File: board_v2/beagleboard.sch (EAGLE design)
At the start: 24 parts, among them U1 DWM1000, X1 5566-2

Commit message: schematiccomplete
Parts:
- removed R7, R8, R9: 0R, rcl:R-EU_R0603
- added IMUCON: B4B-ZR, jst:B4B-ZR
- added X2: 04-JST-B4B-XH-A, bt_con-jst-xh:04-JST-B4B-XH-A
- R4, R5, R6: value 0R -> (none); device rcl:R-EU_R0603 -> rcl:R-EU_R0805
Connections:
- removed net N$10: MOTORL.3, R9.2
- removed net N$11: MOTORL.4, R8.2
- removed net N$4: MOTOTR.2, R4.2
- removed net N$47: U$1.GPIO_45
- removed net N$48: U$1.GPIO_23
- removed net N$49: U$1.GPIO_47
- removed net N$50: U$1.GPIO_27
- removed net N$51: U$1.GPIO_22
- removed net N$52: U$1.GPIO_62
- removed net N$7: MOTOTR.3, R5.2
- removed net N$73: U$1.I2C1_SDA
- removed net N$8: MOTOTR.4, R6.2
- removed net N$82: U$1.AIN5
- removed net N$83: U$1.AIN3
- removed net N$84: U$1.AIN1
- removed net N$9: MOTORL.2, R7.2
- removed net N$96: U$1.I2C1_SCL
- removed net WIPOWER: REGCON.1
- new net CELL1: R4.2, U$1.AIN5, X2-3.1
- new net CELL2: R5.2, U$1.AIN3, X2-2.1
- new net CELL3: R6.2, U$1.AIN1, X2-1.1
- new net MLM0: MOTORL.2, U$1.GPIO_45
- new net MLM1: MOTORL.3, U$1.GPIO_23
- new net MLM2: MOTORL.4, U$1.GPIO_47
- new net MRM0: MOTOTR.2, U$1.GPIO_27
- new net MRM1: MOTOTR.3, U$1.GPIO_22
- new net MRM2: MOTOTR.4, U$1.GPIO_62
- new net SCL1: IMUCON.3, U$1.I2C1_SCL
- new net SDA1: IMUCON.2, U$1.I2C1_SDA
- net +5V: now also IMUCON.1; no longer R4.1, R5.1, R6.1, R7.1, R8.1, R9.1
- net GND: now also IMUCON.4, R4.1, R5.1, R6.1, X2-4.1
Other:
- moved on the sheet: R4, R5, R6

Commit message: main wires
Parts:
- added R7, R8, R9: (no value), rcl:R-EU_R0805
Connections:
- removed net N$17: MCONL.2, MOTORL1.5
- removed net N$19: MCONR.4, MOTORR1.4
- removed net N$20: MCONR.3, MOTORR1.3
- new net N$10: MCONL.1, MOTORL1.5
- new net N$11: MCONL.4, MOTORL1.3
- new net N$4: R7.2, X2-1.1
- new net N$7: R8.2, X2-2.1
- new net N$8: R9.2, X2-3.1
- new net N$9: MCONL.2, MOTORL1.6
- net +3V3: no longer C2.+, REGCON.4
- net +5V: now also C2.+, REGCON.4
- net CELL1: now also R9.1; no longer X2-3.1
- net CELL2: now also R8.1; no longer X2-2.1
- net CELL3: now also R7.1; no longer X2-1.1
- net MRDIR: now also U$1.GPIO_60; no longer U$1.GPIO_51
- net MREN: now also U$1.GPIO_51; no longer U$1.GPIO_60
- net MRM1: now also U$1.GPIO_62; no longer U$1.GPIO_22
- net MRM2: now also U$1.GPIO_22; no longer U$1.GPIO_62
- net N$1: now also MCONL.3; no longer MCONL.4
- net N$12: now also MCONR.2; no longer MCONR.1
- net N$13: now also MCONR.3, MOTORR1.4; no longer MCONL.3, MOTORL1.3
- net N$14: now also MCONR.4, MOTORR1.3; no longer MCONL.1, MOTORL1.6
- net N$15: now also MCONR.1; no longer MCONR.2
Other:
- moved on the sheet: X2-1, X2-2, X2-3, X2-4

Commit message: boardv2 ready to check
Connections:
- net +3V3: no longer U$1.VDD_3V3EXP@1, U$1.VDD_3V3EXP@2
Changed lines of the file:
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@@
 <part name="GND7" library="supply1" deviceset="GND" device=""/>
 <part name="GND8" library="supply1" deviceset="GND" device=""/>
-<part name="+3V1" library="supply1" deviceset="+3V3" device=""/>
 <part name="P+6" library="supply1" deviceset="+5V" device=""/>
-<part name="+3V2" library="supply1" deviceset="+3V3" device=""/>
 <part name="X1" library="con-molex" deviceset="5566-2" device=""/>
 <part name="+3V4" library="supply1" deviceset="+3V3" device=""/>
@@
 <instance part="GND7" gate="1" x="220.98" y="116.84"/>
 <instance part="GND8" gate="1" x="124.46" y="116.84"/>
-<instance part="+3V1" gate="G$1" x="215.9" y="58.42"/>
 <instance part="P+6" gate="1" x="121.92" y="58.42"/>
-<instance part="+3V2" gate="G$1" x="129.54" y="58.42"/>
 <instance part="X1" gate="-1" x="-17.78" y="101.6" rot="R180"/>
 <instance part="X1" gate="-2" x="-17.78" y="106.68" rot="R180"/>
@@
 </segment>
 <segment>
-<pinref part="U$1" gate="G$1" pin="VDD_3V3EXP@1"/>
-<wire x1="144.78" y1="50.8" x2="129.54" y2="50.8" width="0.1524" layer="91"/>
-<wire x1="129.54" y1="50.8" x2="129.54" y2="55.88" width="0.1524" layer="91"/>
-<pinref part="+3V2" gate="G$1" pin="+3V3"/>
-</segment>
-<segment>
-<pinref part="U$1" gate="G$1" pin="VDD_3V3EXP@2"/>
-<wire x1="200.66" y1="50.8" x2="215.9" y2="50.8" width="0.1524" layer="91"/>
-<pinref part="+3V1" gate="G$1" pin="+3V3"/>
-<wire x1="215.9" y1="50.8" x2="215.9" y2="55.88" width="0.1524" layer="91"/>
-</segment>
-<segment>

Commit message: added distance sensor connectors
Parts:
- added SENS1, SENS3, SENS4: B4B-ZR, jst:B4B-ZR
- renumbered IMUCON to SENS2
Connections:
- removed net N$100: U$1.GPIO_117
- removed net N$74: U$1.I2C2_SDA
- removed net N$75: U$1.UART2_RXD
- removed net N$76: U$1.UART1_TXD
- removed net N$77: U$1.UART1_RXD
- removed net N$97: U$1.I2C2_SCL
- removed net N$98: U$1.UART2_TXD
- removed net N$99: U$1.GPIO_49
- new net D1ECHO: SENS1.3, U$1.UART1_TXD
- new net D1TRIG: SENS1.4, U$1.UART1_RXD
- new net D2ECHO: SENS2.3, U$1.UART2_TXD
- new net D2TRIG: SENS2.4, U$1.UART2_RXD
- new net D3ECHO: SENS3.3, U$1.GPIO_49
- new net D3TRIG: SENS3.4, U$1.GPIO_117
- new net D4ECHO: SENS4.3, U$1.I2C2_SCL
- new net D4TRIG: SENS4.4, U$1.I2C2_SDA
- net +5V: now also SENS1.1, SENS3.1, SENS4.1
- net GND: now also SENS1.2, SENS2.2, SENS3.2, SENS4.2; no longer SENS2.4
- net SCL1: no longer SENS2.3
- net SDA1: no longer SENS2.2
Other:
- moved on the sheet: R4, R5, R6, R7, R8, R9, X2-1, X2-2, X2-3, X2-4

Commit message: gpioadjustment
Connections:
- removed net N$105: U$1.AIN6
- removed net N$106: U$1.AIN2
- removed net N$107: U$1.AIN0
- removed net N$45: U$1.TIMER4
- removed net N$46: U$1.TIMER5
- removed net N$69: U$1.SYS_RESETN
- removed net N$92: U$1.PWR_BUT
- new net N$17: U$1.GPIO_22
- new net N$19: U$1.GPIO_62
- net +3V3: no longer U$1.VDD_ADC
- net D3TRIG: now also U$1.AIN6; no longer U$1.GPIO_117
- net D4ECHO: now also U$1.AIN0; no longer U$1.I2C2_SCL
- net D4TRIG: now also U$1.AIN2; no longer U$1.I2C2_SDA
- net MLM0: now also U$1.TIMER4; no longer U$1.GPIO_45
- net MLM1: now also U$1.TIMER5; no longer U$1.GPIO_23
- net MLM2: now also U$1.GPIO_45; no longer U$1.GPIO_47
- net MRM0: now also U$1.GPIO_23; no longer U$1.GPIO_27
- net MRM1: now also U$1.GPIO_47; no longer U$1.GPIO_62
- net MRM2: now also U$1.GPIO_27; no longer U$1.GPIO_22
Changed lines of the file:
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@@
 <?xml version="1.0" encoding="utf-8"?>
 <!DOCTYPE eagle SYSTEM "eagle.dtd">
-<eagle version="7.1.0">
+<eagle version="7.7.0">
 <drawing>
 <settings>
@@
 <part name="P+6" library="supply1" deviceset="+5V" device=""/>
 <part name="X1" library="con-molex" deviceset="5566-2" device=""/>
-<part name="+3V4" library="supply1" deviceset="+3V3" device=""/>
 <part name="SENS2" library="jst" deviceset="B4B-ZR" device=""/>
 <part name="P+7" library="supply1" deviceset="+5V" device=""/>
@@
 <instance part="X1" gate="-1" x="-17.78" y="101.6" rot="R180"/>
 <instance part="X1" gate="-2" x="-17.78" y="106.68" rot="R180"/>
-<instance part="+3V4" gate="G$1" x="220.98" y="20.32"/>
 <instance part="SENS2" gate="G$1" x="71.12" y="116.84" rot="R90"/>
 <instance part="P+7" gate="1" x="63.5" y="106.68"/>
@@
 <junction x="60.96" y="71.12"/>
 </segment>
-<segment>
-<pinref part="U$1" gate="G$1" pin="VDD_ADC"/>
-<wire x1="200.66" y1="15.24" x2="220.98" y2="15.24" width="0.1524" layer="91"/>
-<wire x1="220.98" y1="15.24" x2="220.98" y2="17.78" width="0.1524" layer="91"/>
-<pinref part="+3V4" gate="G$1" pin="+3V3"/>
-</segment>
 </net>
 <net name="N$2" class="0">
@@
 </segment>
 <segment>
+<pinref part="U$1" gate="G$1" pin="GPIO_23"/>
+<wire x1="144.78" y1="104.14" x2="134.62" y2="104.14" width="0.1524" layer="91"/>
+<label x="134.62" y="104.14" size="1.27" layer="95" rot="R180" xref="yes"/>
+</segment>
+</net>
+<net name="MRM1" class="0">
+<segment>
+<pinref part="MOTOTR" gate="A" pin="3"/>
+<wire x1="58.42" y1="-5.08" x2="66.04" y2="-5.08" width="0.1524" layer="91"/>
+<label x="58.42" y="-5.08" size="1.27" layer="95" rot="R180" xref="yes"/>
+</segment>
+<segment>
+<pinref part="U$1" gate="G$1" pin="GPIO_47"/>
+<wire x1="144.78" y1="101.6" x2="134.62" y2="101.6" width="0.1524" layer="91"/>
+<label x="134.62" y="101.6" size="1.27" layer="95" rot="R180" xref="yes"/>
+</segment>
+</net>
+<net name="MRM2" class="0">
+<segment>
+<pinref part="MOTOTR" gate="A" pin="4"/>
+<wire x1="58.42" y1="-7.62" x2="66.04" y2="-7.62" width="0.1524" layer="91"/>
+<label x="58.42" y="-7.62" size="1.27" layer="95" rot="R180" xref="yes"/>
+</segment>
+<segment>
 <pinref part="U$1" gate="G$1" pin="GPIO_27"/>
 <wire x1="144.78" y1="99.06" x2="134.62" y2="99.06" width="0.1524" layer="91"/>
@@
 </segment>
 </net>
-<net name="MRM1" class="0">
-<segment>
-<pinref part="MOTOTR" gate="A" pin="3"/>
-<wire x1="58.42" y1="-5.08" x2="66.04" y2="-5.08" width="0.1524" layer="91"/>
-<label x="58.42" y="-5.08" size="1.27" layer="95" rot="R180" xref="yes"/>
-</segment>
-<segment>
-<pinref part="U$1" gate="G$1" pin="GPIO_62"/>
-<wire x1="144.78" y1="93.98" x2="134.62" y2="93.98" width="0.1524" layer="91"/>
-<label x="134.62" y="93.98" size="1.27" layer="95" rot="R180" xref="yes"/>
-</segment>
-</net>
-<net name="MRM2" class="0">
-<segment>
-<pinref part="MOTOTR" gate="A" pin="4"/>
-<wire x1="58.42" y1="-7.62" x2="66.04" y2="-7.62" width="0.1524" layer="91"/>
-<label x="58.42" y="-7.62" size="1.27" layer="95" rot="R180" xref="yes"/>
-</segment>
-<segment>
-<pinref part="U$1" gate="G$1" pin="GPIO_22"/>
-<wire x1="144.78" y1="96.52" x2="134.62" y2="96.52" width="0.1524" layer="91"/>
-<label x="134.62" y="96.52" size="1.27" layer="95" rot="R180" xref="yes"/>
-</segment>
-</net>
 <net name="MLM0" class="0">
 <segment>
@@
 </segment>
 <segment>
+<pinref part="U$1" gate="G$1" pin="TIMER4"/>
+<wire x1="144.78" y1="111.76" x2="134.62" y2="111.76" width="0.1524" layer="91"/>
+<label x="134.62" y="111.76" size="1.27" layer="95" rot="R180" xref="yes"/>
+</segment>
+</net>
+<net name="MLM1" class="0">
+<segment>
+<pinref part="MOTORL" gate="A" pin="3"/>
+<wire x1="-2.54" y1="-5.08" x2="5.08" y2="-5.08" width="0.1524" layer="91"/>
+<label x="-2.54" y="-5.08" size="1.27" layer="95" rot="R180" xref="yes"/>
+</segment>
+<segment>
+<pinref part="U$1" gate="G$1" pin="TIMER5"/>
+<wire x1="144.78" y1="109.22" x2="134.62" y2="109.22" width="0.1524" layer="91"/>
+<label x="134.62" y="109.22" size="1.27" layer="95" rot="R180" xref="yes"/>
+</segment>
+</net>
+<net name="MLM2" class="0">
+<segment>
+<pinref part="MOTORL" gate="A" pin="4"/>
+<wire x1="-2.54" y1="-7.62" x2="5.08" y2="-7.62" width="0.1524" layer="91"/>
+<label x="-2.54" y="-7.62" size="1.27" layer="95" rot="R180" xref="yes"/>
+</segment>
+<segment>
 <pinref part="U$1" gate="G$1" pin="GPIO_45"/>
 <wire x1="144.78" y1="106.68" x2="134.62" y2="106.68" width="0.1524" layer="91"/>
@@
 </segment>
 </net>
-<net name="MLM1" class="0">
-<segment>
-<pinref part="MOTORL" gate="A" pin="3"/>
-<wire x1="-2.54" y1="-5.08" x2="5.08" y2="-5.08" width="0.1524" layer="91"/>
-<label x="-2.54" y="-5.08" size="1.27" layer="95" rot="R180" xref="yes"/>
-</segment>
-<segment>
-<pinref part="U$1" gate="G$1" pin="GPIO_23"/>
-<wire x1="144.78" y1="104.14" x2="134.62" y2="104.14" width="0.1524" layer="91"/>
-<label x="134.62" y="104.14" size="1.27" layer="95" rot="R180" xref="yes"/>
-</segment>
-</net>
-<net name="MLM2" class="0">
-<segment>
-<pinref part="MOTORL" gate="A" pin="4"/>
-<wire x1="-2.54" y1="-7.62" x2="5.08" y2="-7.62" width="0.1524" layer="91"/>
-<label x="-2.54" y="-7.62" size="1.27" layer="95" rot="R180" xref="yes"/>
-</segment>
-<segment>
-<pinref part="U$1" gate="G$1" pin="GPIO_47"/>
-<wire x1="144.78" y1="101.6" x2="134.62" y2="101.6" width="0.1524" layer="91"/>
-<label x="134.62" y="101.6" size="1.27" layer="95" rot="R180" xref="yes"/>
-</segment>
-</net>
 <net name="N$18" class="0">
 <segment>
@@
 </segment>
 </net>
-<net name="N$45" class="0">
-<segment>
-<pinref part="U$1" gate="G$1" pin="TIMER4"/>
-<wire x1="144.78" y1="111.76" x2="134.62" y2="111.76" width="0.1524" layer="91"/>
-</segment>
-</net>
-<net name="N$46" class="0">
-<segment>
-<pinref part="U$1" gate="G$1" pin="TIMER5"/>
-<wire x1="144.78" y1="109.22" x2="134.62" y2="109.22" width="0.1524" layer="91"/>
-</segment>
-</net>
 <net name="N$53" class="0">
 <segment>
@@
 </segment>
 </net>
-<net name="N$69" class="0">
-<segment>
-<pinref part="U$1" gate="G$1" pin="SYS_RESETN"/>
-<wire x1="200.66" y1="43.18" x2="210.82" y2="43.18" width="0.1524" layer="91"/>
-</segment>
-</net>
 <net name="D4TRIG" class="0">
-<segment>
-<pinref part="U$1" gate="G$1" pin="I2C2_SDA"/>
-<wire x1="200.66" y1="30.48" x2="210.82" y2="30.48" width="0.1524" layer="91"/>
-<label x="210.82" y="30.48" size="1.016" layer="95" xref="yes"/>
-</segment>
 <segment>
 <pinref part="SENS4" gate="G$1" pin="4"/>
 <wire x1="116.84" y1="109.22" x2="116.84" y2="104.14" width="0.1524" layer="91"/>
 <label x="116.84" y="104.14" size="1.016" layer="95" rot="R270" xref="yes"/>
+</segment>
+<segment>
+<pinref part="U$1" gate="G$1" pin="AIN2"/>
+<wire x1="144.78" y1="7.62" x2="134.62" y2="7.62" width="0.1524" layer="91"/>
+<label x="134.62" y="7.62" size="1.27" layer="95" rot="R180" xref="yes"/>
 </segment>
 </net>
@@
 </segment>
 </net>
-<net name="N$92" class="0">
-<segment>
-<pinref part="U$1" gate="G$1" pin="PWR_BUT"/>
-<wire x1="144.78" y1="43.18" x2="134.62" y2="43.18" width="0.1524" layer="91"/>
-</segment>
-</net>
 <net name="D4ECHO" class="0">
-<segment>
-<pinref part="U$1" gate="G$1" pin="I2C2_SCL"/>
-<wire x1="144.78" y1="30.48" x2="134.62" y2="30.48" width="0.1524" layer="91"/>
-<label x="134.62" y="30.48" size="1.016" layer="95" rot="R180" xref="yes"/>
-</segment>
 <segment>
 <pinref part="SENS4" gate="G$1" pin="3"/>
@@
 <label x="114.3" y="104.14" size="1.016" layer="95" rot="R270" xref="yes"/>
 </segment>
+<segment>
+<pinref part="U$1" gate="G$1" pin="AIN0"/>
+<wire x1="144.78" y1="5.08" x2="134.62" y2="5.08" width="0.1524" layer="91"/>
+<label x="134.62" y="5.08" size="1.27" layer="95" rot="R180" xref="yes"/>
+</segment>
 </net>
 <net name="D2ECHO" class="0">
@@
 </segment>
 <segment>
-<pinref part="U$1" gate="G$1" pin="GPIO_117"/>
-<wire x1="144.78" y1="22.86" x2="134.62" y2="22.86" width="0.1524" layer="91"/>
-<label x="134.62" y="22.86" size="1.016" layer="95" rot="R180" xref="yes"/>
+<pinref part="U$1" gate="G$1" pin="AIN6"/>
+<wire x1="144.78" y1="10.16" x2="134.62" y2="10.16" width="0.1524" layer="91"/>
+<label x="134.62" y="10.16" size="1.27" layer="95" rot="R180" xref="yes"/>
 </segment>
 </net>
@@
 <pinref part="U$1" gate="G$1" pin="AIN4"/>
 <wire x1="144.78" y1="12.7" x2="134.62" y2="12.7" width="0.1524" layer="91"/>
-</segment>
-</net>
-<net name="N$105" class="0">
-<segment>
-<pinref part="U$1" gate="G$1" pin="AIN6"/>
-<wire x1="144.78" y1="10.16" x2="134.62" y2="10.16" width="0.1524" layer="91"/>
-</segment>
-</net>
-<net name="N$106" class="0">
-<segment>
-<pinref part="U$1" gate="G$1" pin="AIN2"/>
-<wire x1="144.78" y1="7.62" x2="134.62" y2="7.62" width="0.1524" layer="91"/>
-</segment>
-</net>
-<net name="N$107" class="0">
-<segment>
-<pinref part="U$1" gate="G$1" pin="AIN0"/>
-<wire x1="144.78" y1="5.08" x2="134.62" y2="5.08" width="0.1524" layer="91"/>
 </segment>
 </net>
@@
 </segment>
 </net>
+<net name="N$17" class="0">
+<segment>
+<pinref part="U$1" gate="G$1" pin="GPIO_22"/>
+<wire x1="144.78" y1="96.52" x2="134.62" y2="96.52" width="0.1524" layer="91"/>
+</segment>
+</net>
+<net name="N$19" class="0">
+<segment>
+<pinref part="U$1" gate="G$1" pin="GPIO_62"/>
+<wire x1="144.78" y1="93.98" x2="134.62" y2="93.98" width="0.1524" layer="91"/>
+</segment>
+</net>

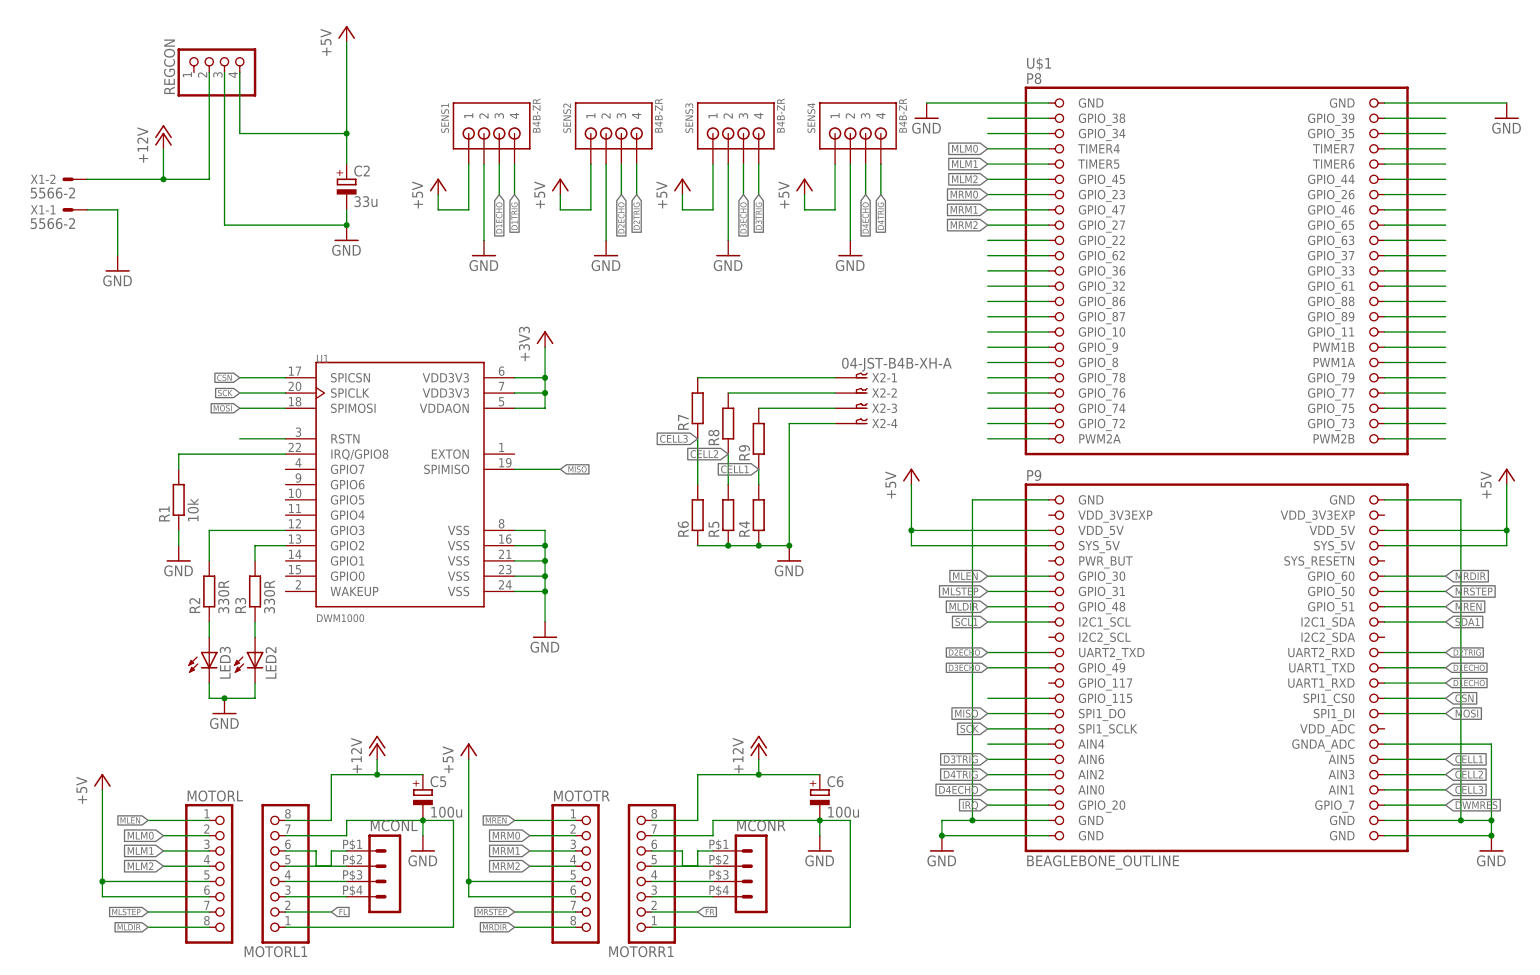
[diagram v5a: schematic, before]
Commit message: check and reconfigure gpios
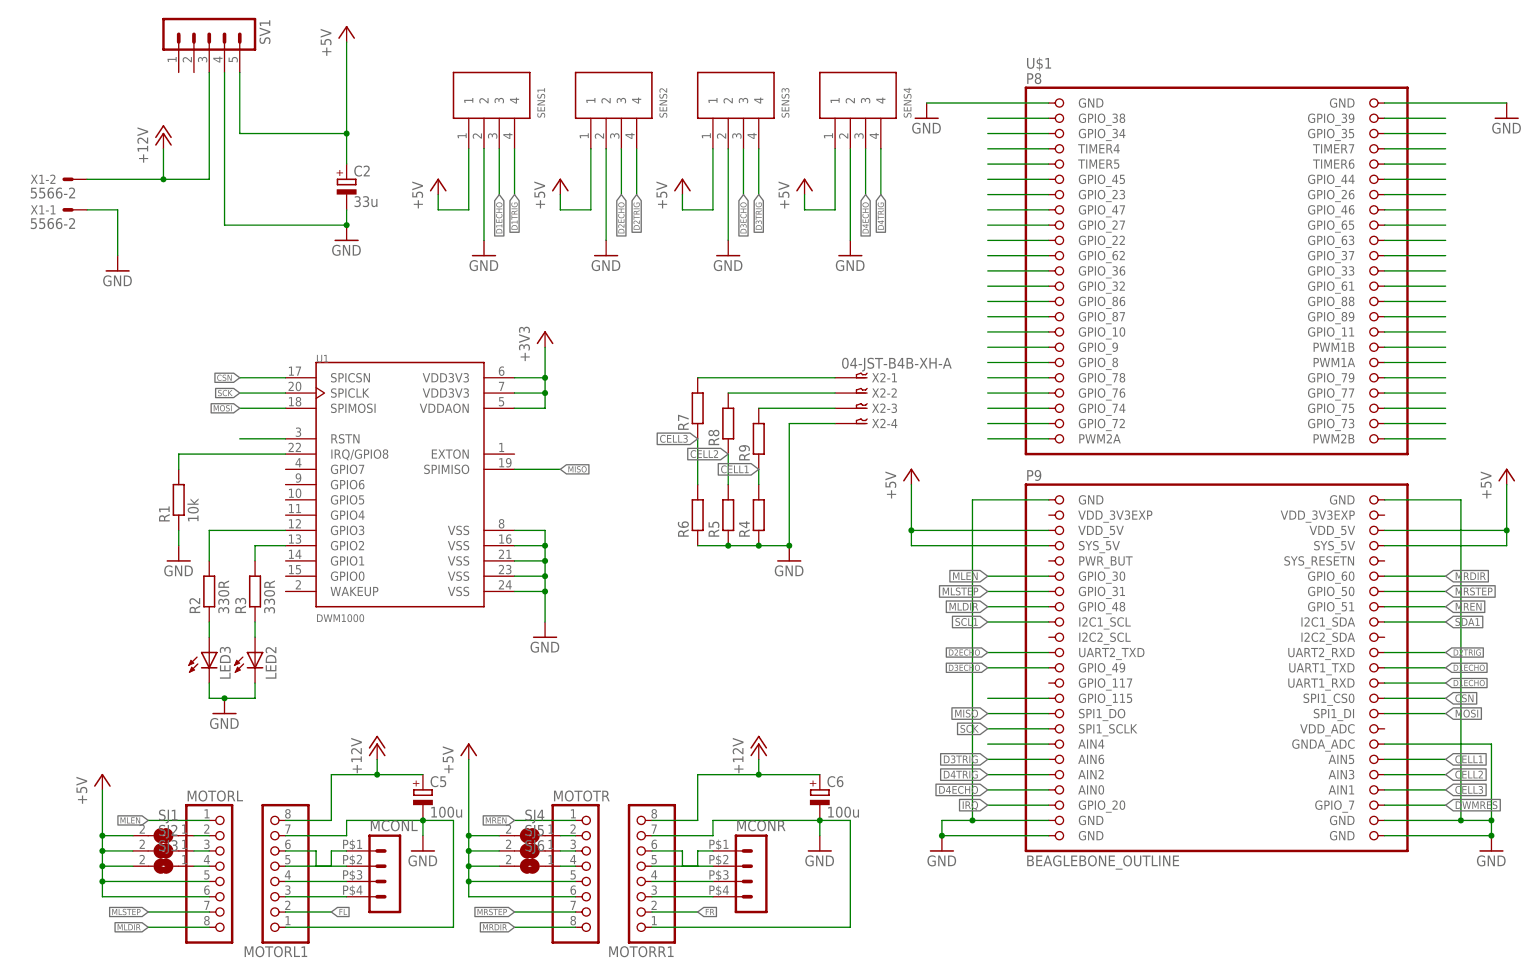
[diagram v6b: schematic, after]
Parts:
- removed REGCON: (no value), pinhead:PINHD-1X4
- added SJ1, SJ2, SJ3, SJ4, SJ5, SJ6: (no value), jumper:SJ
- added SV1: (no value), con-lstb:MA05-1
- SENS1, SENS2, SENS3, SENS4: value B4B-ZR -> 4PIN; device jst:B4B-ZR -> libsjst_eph:4PIN
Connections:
- removed net MLM0: MOTORL.2, U$1.TIMER4
- removed net MLM1: MOTORL.3, U$1.TIMER5
- removed net MLM2: MOTORL.4, U$1.GPIO_45
- removed net MRM0: MOTOTR.2, U$1.GPIO_23
- removed net MRM1: MOTOTR.3, U$1.GPIO_47
- removed net MRM2: MOTOTR.4, U$1.GPIO_27
- new net N$20: U$1.TIMER4
- new net N$42: U$1.TIMER5
- new net N$43: U$1.GPIO_45
- new net N$44: U$1.GPIO_23
- new net N$45: U$1.GPIO_47
- new net N$46: U$1.GPIO_27
- new net N$52: MOTORL.4, SJ3.1
- new net N$53: MOTORL.3, SJ2.1
- new net N$54: MOTORL.2, SJ1.1
- new net N$55: MOTOTR.2, SJ4.1
- new net N$65: MOTOTR.3, SJ5.1
- new net N$66: MOTOTR.4, SJ6.1
- net +12V: now also SV1.3; no longer REGCON.2
- net +5V: now also SJ1.2, SJ2.2, SJ3.2, SJ4.2, SJ5.2, SJ6.2, SV1.5; no longer REGCON.4
- net GND: now also SV1.4; no longer REGCON.3
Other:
- moved on the sheet: SENS1, SENS2, SENS3, SENS4
